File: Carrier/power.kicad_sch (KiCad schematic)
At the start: 36 parts, among them J8 USB_C_Receptacle_USB2.0_16P, Q1 AO3400A, Q3 AO3400A, U12 USBLC6-2SC6, U2 IP5306

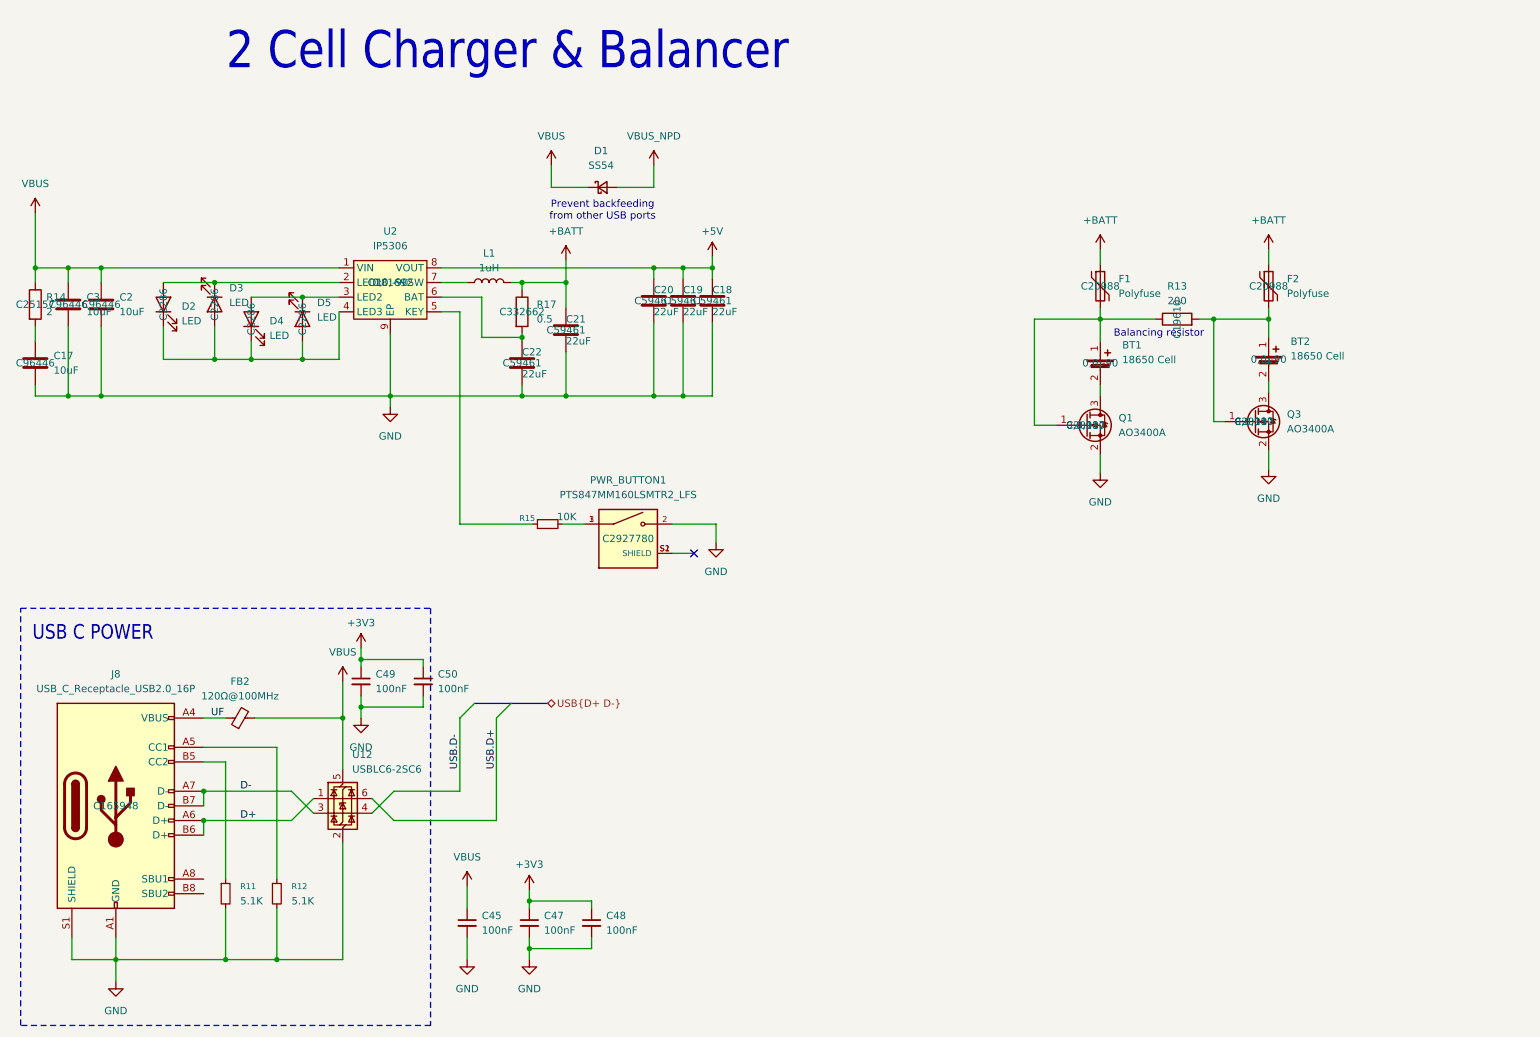
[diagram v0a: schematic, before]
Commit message: fix: sync schematic prot3 and v2.5
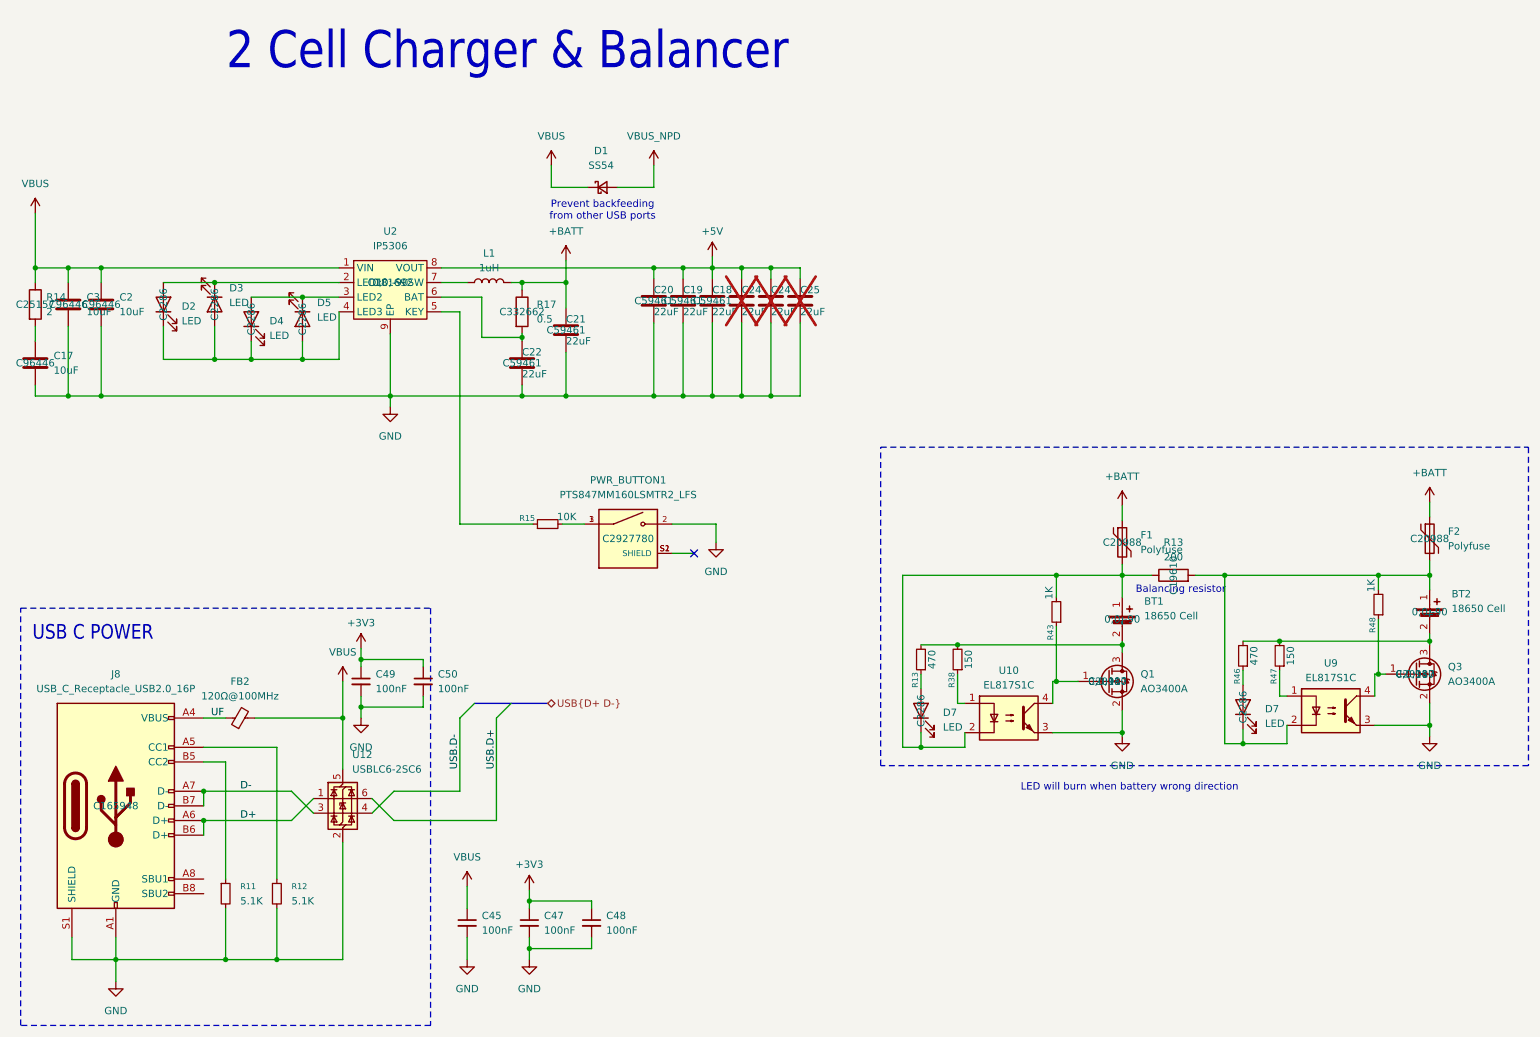
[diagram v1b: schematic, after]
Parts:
- added C24 (x2), C25: 22uF, Capacitor_SMD:C_0603_1608Metric, symbol Device:C
- added D7 (x2): LED, LED_SMD:LED_0603_1608Metric, symbol Device:LED
- added R13, R46: 470, Resistor_SMD:R_0402_1005Metric, symbol Device:R_Small
- added R38, R47: 150, Resistor_SMD:R_0402_1005Metric, symbol Device:R_Small
- added R43, R48: 1K, Resistor_SMD:R_0402_1005Metric, symbol Device:R_Small
- added U10, U9: EL817S1C, EL817:SOIC254P1030X390-4N, symbol Isolator:EL817
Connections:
- net +5V: now also C24.1, C24.1, C25.1
- net GND: now also C24.2, C24.2, C25.2, U10.3, U9.3
- net at BT1.1 (+), F1.2, R13.1: now also D7.1 (K), R43.2, U10.2; no longer Q1.1 (G)
- net at BT2.1 (+), F2.2, R13.2: now also D7.1 (K), R48.2, U9.2; no longer Q3.1 (G)
- net at BT2.2 (-), Q3.3 (D): now also R46.2, R47.2
- net at BT1.2 (-), Q1.3 (D): now also R13.2, R38.2
- new net: D7.2 (A), R46.1
- new net: R47.1, U9.1
- new net: Q3.1 (G), R48.1, U9.4
- new net: D7.2 (A), R13.1
- new net: Q1.1 (G), R43.1, U10.4
- new net: R38.1, U10.1
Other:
- note added: "LED will burn when battery wrong direction"
- moved on the sheet: BT1, BT2, F1, F2, Q1, Q3, R13

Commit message: fix annotation
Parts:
- renumbered C24 to C?, D7 to D8, R13 to R?
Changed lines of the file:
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@@
 		(dnp no)
 		(fields_autoplaced yes)
-		(property "Reference" "D7"
-			(at 234.315 137.4774 90)
+		(property "Reference" "D8"
+			(at 233.68 136.2074 90)
 			(effects
 				(font
@@
 		)
 		(property "Value" "LED"
-			(at 234.315 140.0174 90)
+			(at 233.68 138.7474 90)
 			(effects
 				(font
@@
 		)
 		(property "LCSC" "C2286"
-			(at 230.505 137.16 0)
+			(at 233.68 141.2874 90)
 			(effects
 				(font
 					(size 1.27 1.27)
 				)
+				(justify right)
 			)
 		)
@@
 			(project "badgeCarrierCard"
 				(path "/d0a98fce-b133-4503-8f8a-83b2a1eed591/05158df8-c1e6-40b8-af8c-4aba99cbc568"
-					(reference "D7")
+					(reference "D8")
 					(unit 1)
 				)
@@
 		(fields_autoplaced yes)
 		(property "Reference" "D7"
-			(at 178.435 138.1124 90)
+			(at 177.8 136.8424 90)
 			(effects
 				(font
@@
 		)
 		(property "Value" "LED"
-			(at 178.435 140.6524 90)
+			(at 177.8 139.3824 90)
 			(effects
 				(font
@@
 		)
 		(property "LCSC" "C2286"
-			(at 174.625 137.795 0)
+			(at 177.8 141.9224 90)
 			(effects
 				(font
 					(size 1.27 1.27)
 				)
+				(justify right)
 			)
 		)
@@
 		(on_board yes)
 		(dnp no)
-		(property "Reference" "R13"
+		(property "Reference" "R?"
 			(at 173.609 132.461 90)
 			(effects
@@
 			(project "badgeCarrierCard"
 				(path "/d0a98fce-b133-4503-8f8a-83b2a1eed591/05158df8-c1e6-40b8-af8c-4aba99cbc568"
-					(reference "R13")
+					(reference "R?")
 					(unit 1)
 				)
@@
 		(on_board yes)
 		(dnp yes)
-		(property "Reference" "C24"
+		(property "Reference" "C?"
 			(at 143.51 64.77 0)
 			(effects
@@
 			(project "badgeCarrierCard"
 				(path "/d0a98fce-b133-4503-8f8a-83b2a1eed591/05158df8-c1e6-40b8-af8c-4aba99cbc568"
-					(reference "C24")
+					(reference "C?")
 					(unit 1)
 				)

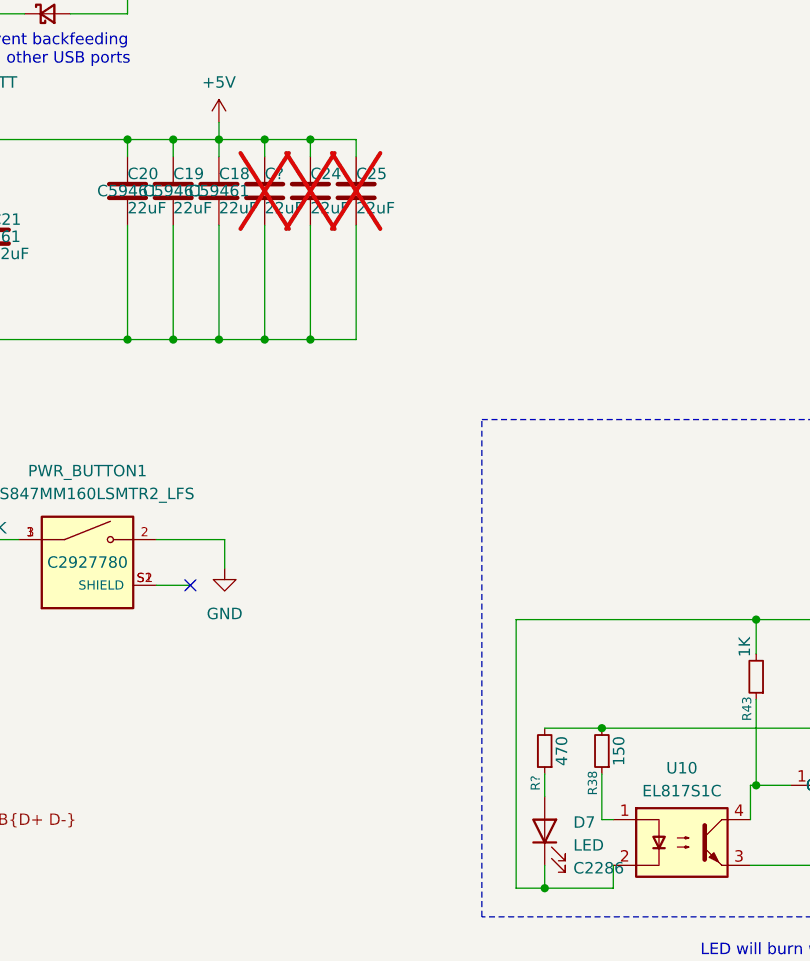
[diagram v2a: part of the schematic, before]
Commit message: push resistor name
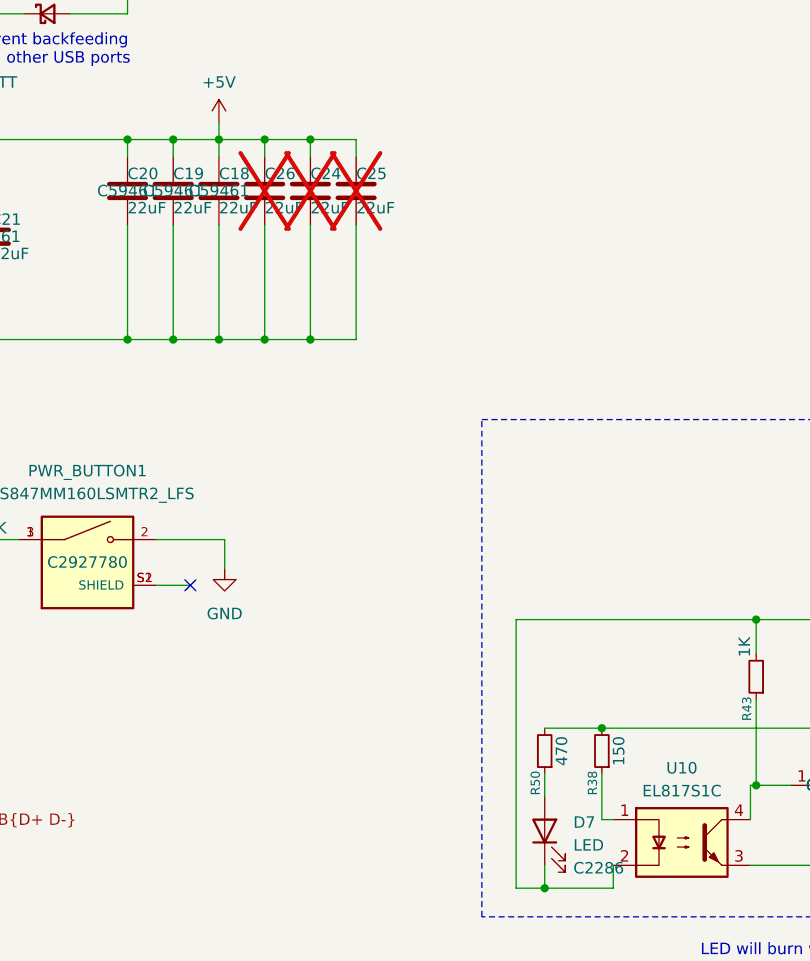
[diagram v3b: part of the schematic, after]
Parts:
- gave numbers to parts that had none: 2
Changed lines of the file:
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@@
 		(on_board yes)
 		(dnp no)
-		(property "Reference" "R?"
+		(property "Reference" "R50"
 			(at 173.609 132.461 90)
 			(effects
@@
 			(project "badgeCarrierCard"
 				(path "/d0a98fce-b133-4503-8f8a-83b2a1eed591/05158df8-c1e6-40b8-af8c-4aba99cbc568"
-					(reference "R?")
+					(reference "R50")
 					(unit 1)
 				)
@@
 		(on_board yes)
 		(dnp yes)
-		(property "Reference" "C?"
+		(property "Reference" "C26"
 			(at 143.51 64.77 0)
 			(effects
@@
 			(project "badgeCarrierCard"
 				(path "/d0a98fce-b133-4503-8f8a-83b2a1eed591/05158df8-c1e6-40b8-af8c-4aba99cbc568"
-					(reference "C?")
+					(reference "C26")
 					(unit 1)
 				)

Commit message: chore: lib cleanup
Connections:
- no-connect marks 1 -> 3
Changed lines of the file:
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@@
+	)
+	(no_connect
+		(at 50.165 167.005)
 	)
 	(no_connect
 		(at 135.255 110.49)
 	)
+	(no_connect
+		(at 50.165 169.545)
+	)
 	(bus_entry

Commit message: fix: new smd footprint for button
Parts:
- PWR_BUTTON1: footprint PTS847MM160LSMTR2_LFS:SW_PTS847MM160LSMTR2_LFS -> PTS847MM160LSMTR2_LFS:SW_PTS847MM160SMTR2_LFS
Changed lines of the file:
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@@
 			)
 		)
-		(property "Footprint" "PTS847MM160LSMTR2_LFS:SW_PTS847MM160LSMTR2_LFS"
+		(property "Footprint" "PTS847MM160LSMTR2_LFS:SW_PTS847MM160SMTR2_LFS"
 			(at 123.825 107.95 0)
 			(effects

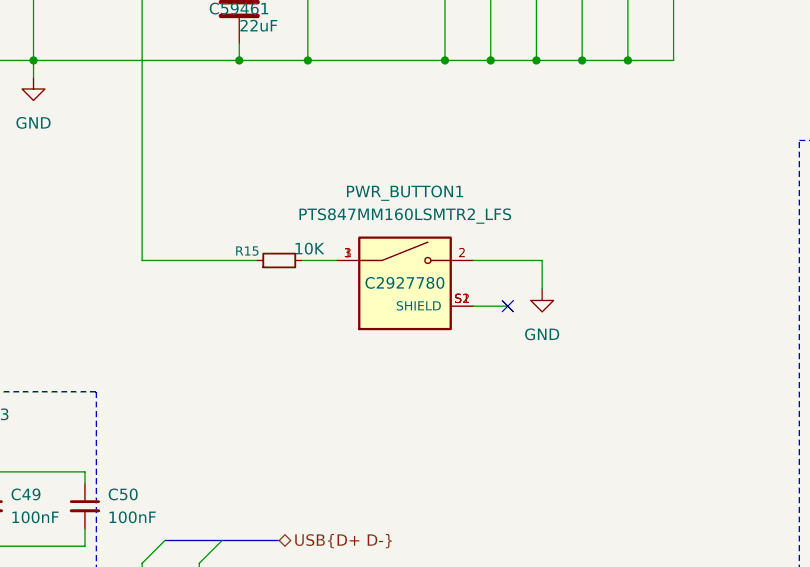
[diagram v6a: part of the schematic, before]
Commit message: Moved lcd screen connector for new screen, corrected LCSC partnumbers
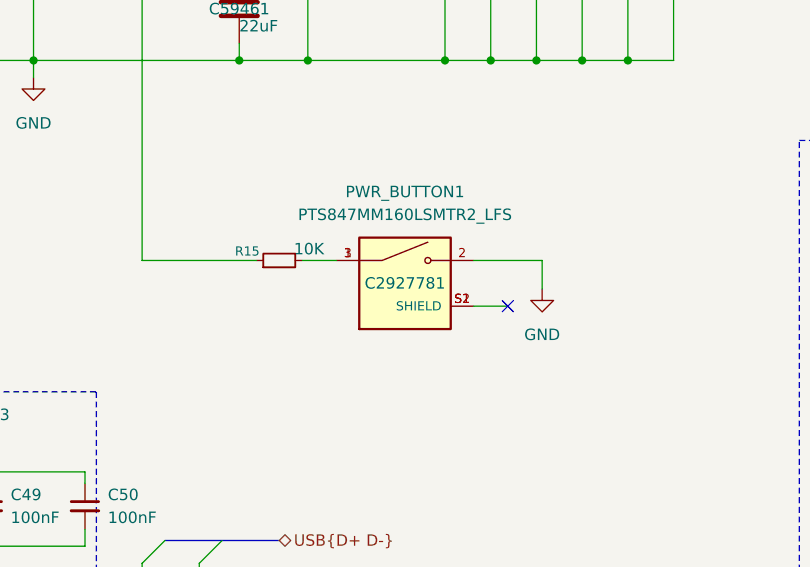
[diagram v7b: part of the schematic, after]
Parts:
- PWR_BUTTON1: LCSC C2927780 -> C2927781
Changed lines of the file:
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@@
 			)
 		)
-		(property "LCSC" "C2927780"
+		(property "LCSC" "C2927781"
 			(at 123.825 107.95 0)
 			(effects
